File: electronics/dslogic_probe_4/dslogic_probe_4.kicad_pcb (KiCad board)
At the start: 2 copper layers, 16 parts, among them J1 Conn_02x04_Odd_Even, J2 Conn_02x04_Odd_Even

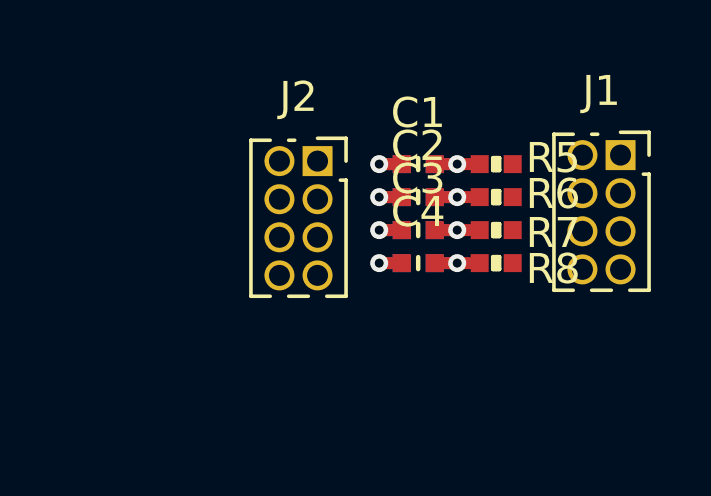
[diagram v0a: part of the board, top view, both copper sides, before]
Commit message: edge footprints for probes
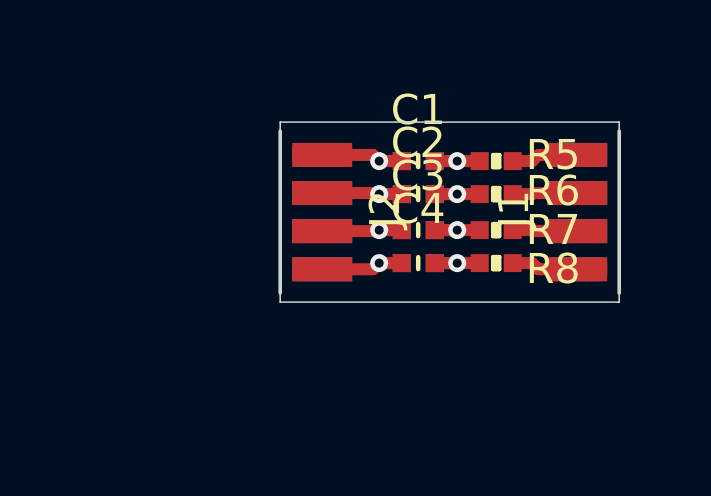
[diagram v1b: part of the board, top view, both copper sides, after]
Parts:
- J1, J2: footprint Connector_PinSocket_1.27mm:PinSocket_2x04_P1.27mm_Vertical -> SquantorConnectors:Header-0127-2X04-EDGE
- moved J1 3.18 mm to (161.6, 77.0), turned to 90 degrees
- moved J2 2.11 mm to (155.3, 77.0), turned to -90 degrees
- moved C1 0.10 mm to (157.4, 75.3)
- moved R1 0.10 mm to (157.4, 75.3)
- moved R5 0.10 mm to (160.0, 75.3)
- moved C2 0.10 mm to (157.4, 76.4)
- moved R2 0.10 mm to (157.4, 76.4)
- moved R6 0.10 mm to (160.0, 76.4)
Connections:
- C3 pad 1: Net-(C3-Pad1) -> Net-(J2-Pad6)
- J1 pad 2: Net-(R5-Pad2) -> Net-(R8-Pad2)
- J1 pad 4: Net-(R6-Pad2) -> Net-(R7-Pad2)
- J1 pad 6: Net-(R7-Pad2) -> Net-(R6-Pad2)
- J1 pad 8: Net-(R8-Pad2) -> Net-(R5-Pad2)
- J2 pad 1: Net-(C1-Pad1) -> /GND
- J2 pad 2: /GND -> Net-(C1-Pad1)
- J2 pad 3: Net-(C2-Pad1) -> /GND
- J2 pad 4: /GND -> Net-(C2-Pad1)
- J2 pad 5: Net-(C3-Pad1) -> /GND
- J2 pad 6: /GND -> Net-(J2-Pad6)
- J2 pad 7: Net-(C4-Pad1) -> /GND
- J2 pad 8: /GND -> Net-(C4-Pad1)
- R3 pad 1: Net-(C3-Pad1) -> Net-(J2-Pad6)
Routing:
- net Net-(J2-Pad6): track 0.00 -> 3.41 mm, vias 0 -> 1
- net Net-(R8-Pad2): track 0.00 -> 2.23 mm
- net Net-(R5-Pad2): track 0.00 -> 2.23 mm
- net Net-(R7-Pad2): track 0.00 -> 2.16 mm
- net Net-(R6-Pad2): track 0.00 -> 2.16 mm
- net Net-(C4-Pad1): track 1.50 -> 3.48 mm
- net Net-(C1-Pad1): track 1.50 -> 3.48 mm
- net Net-(C2-Pad1): track 1.50 -> 3.41 mm
- net Net-(C3-Pad1): track 1.50 -> 0.00 mm, vias 1 -> 0
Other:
- board outline added: 11.3 x 6 mm

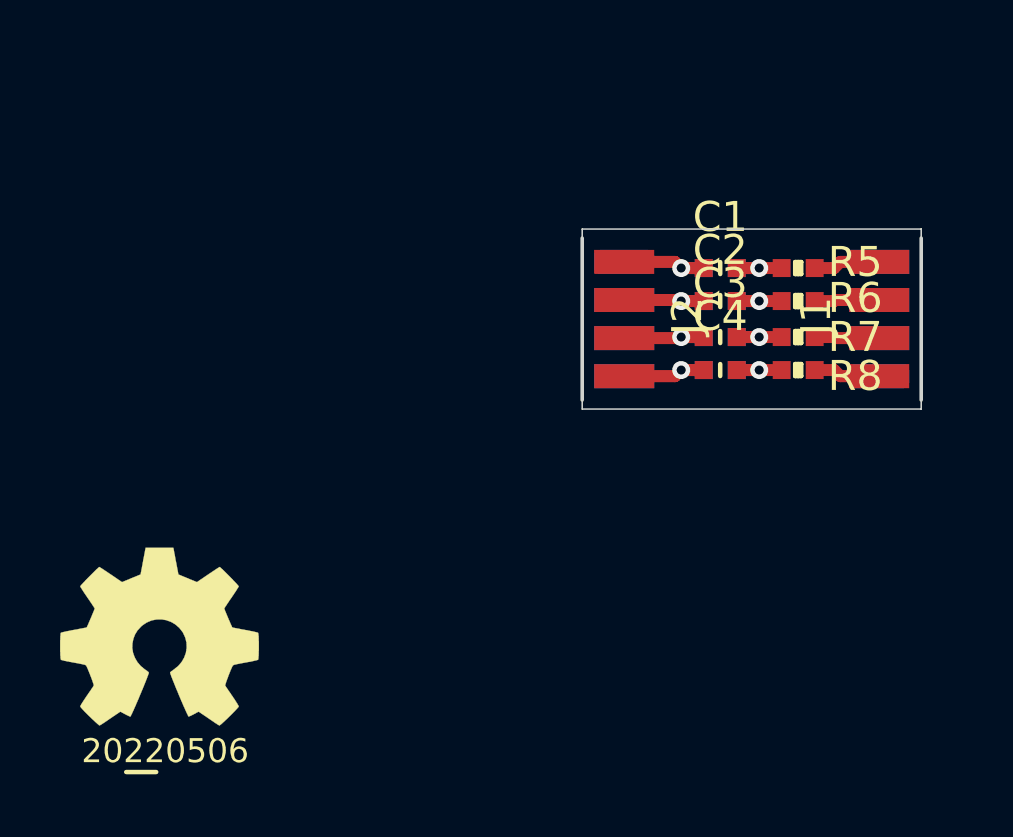
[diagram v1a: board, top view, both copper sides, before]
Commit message: added labels
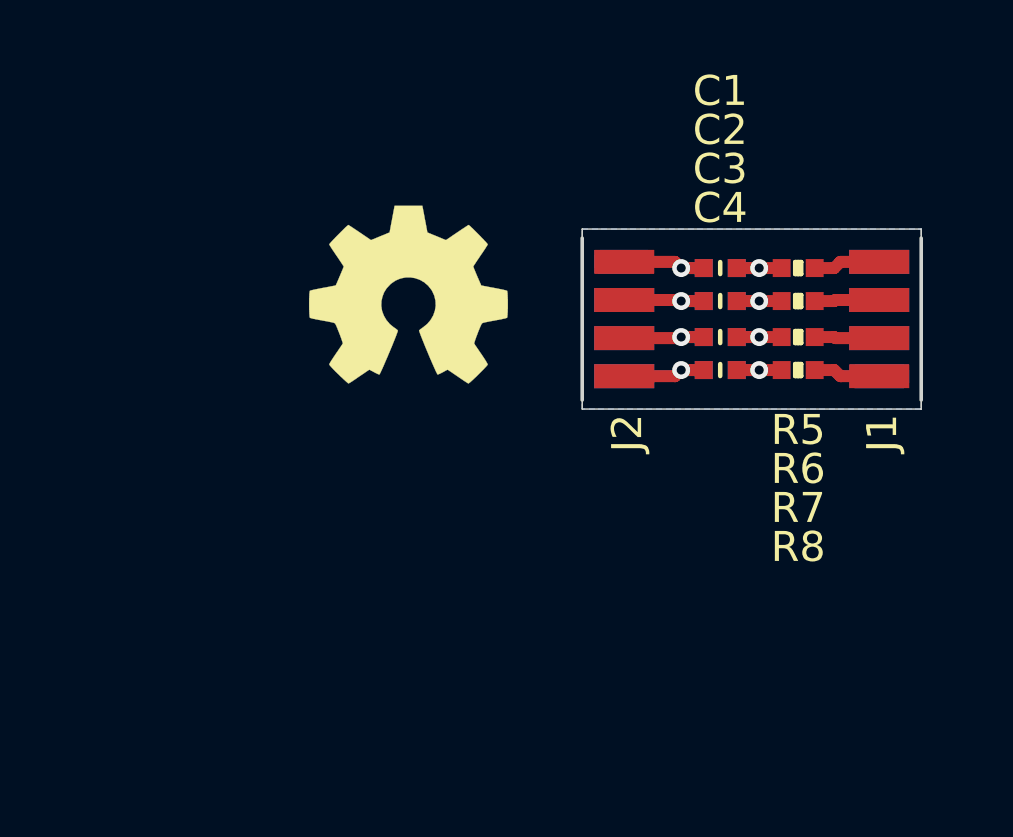
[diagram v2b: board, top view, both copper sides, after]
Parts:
- N1: moved to B.Cu
- moved N1 26.4 mm to (159.6, 76.2), turned to -90 degrees
- moved N2 14.1 mm to (147.0, 76.2)
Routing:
- added copper zone on B.Cu, net /GND
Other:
- board text added: "GND"

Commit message: made unplaceable labels invisible
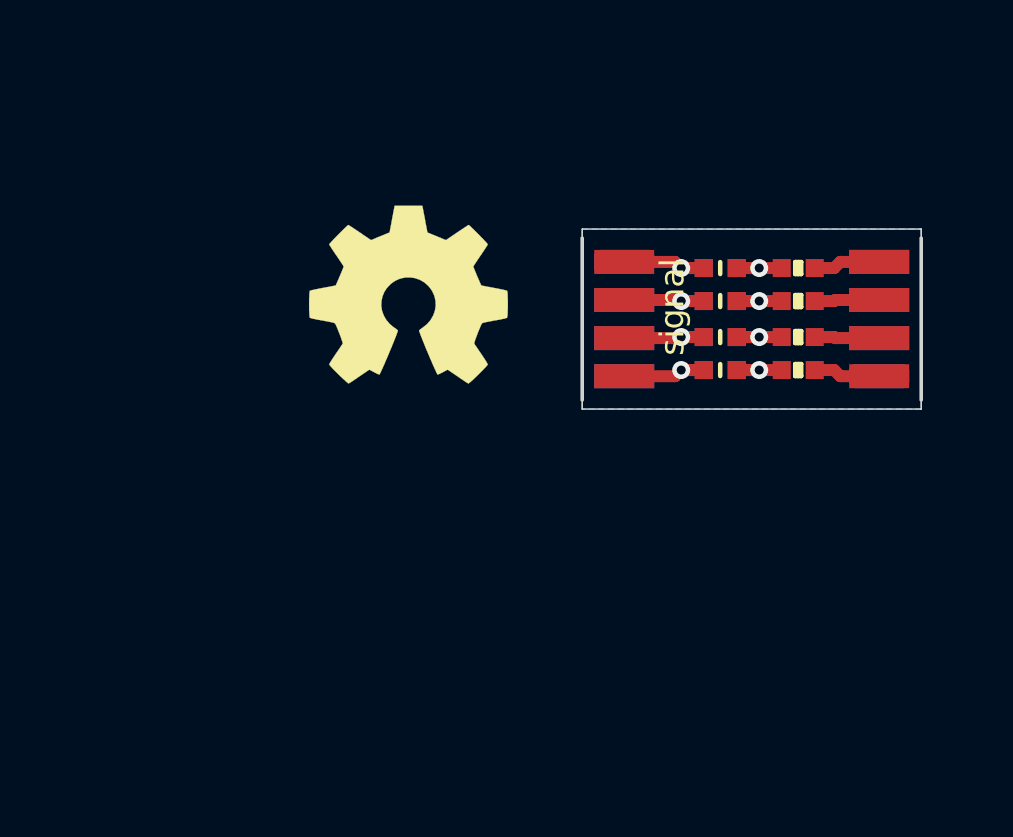
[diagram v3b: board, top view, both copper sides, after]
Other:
- board text added: "signal"
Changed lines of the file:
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@@
     (property "Sheetname" "")
     (attr smd)
-    (fp_text reference "C2" (at 0 -5.7) (layer "F.SilkS")
-      (effects (font (size 1 1) (thickness 0.15)))
-    )
-    (fp_text value "100p" (at 0 -5.7) (layer "F.Fab")
+    (fp_text reference "C2" (at 0 -5.7) (layer "F.Fab")
+      (effects (font (size 1 1) (thickness 0.15)))
+    )
+    (fp_text value "100p" (at -2.8 -5.7) (layer "F.Fab")
       (effects (font (size 1 1) (thickness 0.15)))
     )
@@
     (property "Sheetname" "")
     (attr smd)
-    (fp_text reference "J2" (at 3.8 1 90) (layer "F.SilkS")
+    (fp_text reference "J2" (at 3.8 2.3 90) (layer "F.Fab")
       (effects (font (size 1 1) (thickness 0.15)))
     )
@@
     (property "Sheetname" "")
     (attr smd)
-    (fp_text reference "J1" (at -3.8 1.2 90) (layer "F.SilkS")
+    (fp_text reference "J1" (at -3.8 2.5 90) (layer "F.Fab")
       (effects (font (size 1 1) (thickness 0.15)))
     )
@@
     (property "Sheetname" "")
     (attr smd)
-    (fp_text reference "C3" (at 0 -5.6) (layer "F.SilkS")
-      (effects (font (size 1 1) (thickness 0.15)))
-    )
-    (fp_text value "100p" (at 0 -5.6) (layer "F.Fab")
+    (fp_text reference "C3" (at 0 -5.6) (layer "F.Fab")
+      (effects (font (size 1 1) (thickness 0.15)))
+    )
+    (fp_text value "100p" (at -2.8 -5.6) (layer "F.Fab")
       (effects (font (size 1 1) (thickness 0.15)))
     )
@@
     (property "Sheetname" "")
     (attr smd)
-    (fp_text reference "R7" (at 0 5.7) (layer "F.SilkS")
+    (fp_text reference "R7" (at 2.4 5.7) (layer "F.Fab")
       (effects (font (size 1 1) (thickness 0.15)))
     )
@@
     (property "Sheetname" "")
     (attr smd)
-    (fp_text reference "C1" (at 0 -5.9) (layer "F.SilkS")
-      (effects (font (size 1 1) (thickness 0.15)))
-    )
-    (fp_text value "100p" (at 0 -5.9) (layer "F.Fab")
+    (fp_text reference "C1" (at 0 -5.9) (layer "F.Fab")
+      (effects (font (size 1 1) (thickness 0.15)))
+    )
+    (fp_text value "100p" (at -2.8 -5.9) (layer "F.Fab")
       (effects (font (size 1 1) (thickness 0.15)))
     )
@@
     (property "Sheetname" "")
     (attr smd)
-    (fp_text reference "R5" (at 0 5.4) (layer "F.SilkS")
+    (fp_text reference "R5" (at 2.4 5.4) (layer "F.Fab")
       (effects (font (size 1 1) (thickness 0.15)))
     )
@@
     (property "Sheetname" "")
     (attr smd)
-    (fp_text reference "R6" (at 0 5.6) (layer "F.SilkS")
+    (fp_text reference "R6" (at 2.4 5.6) (layer "F.Fab")
       (effects (font (size 1 1) (thickness 0.15)))
     )
@@
     (property "Sheetname" "")
     (attr smd)
-    (fp_text reference "C4" (at 0 -5.4) (layer "F.SilkS")
-      (effects (font (size 1 1) (thickness 0.15)))
-    )
-    (fp_text value "100p" (at 0 -5.4) (layer "F.Fab")
+    (fp_text reference "C4" (at 0 -5.4) (layer "F.Fab")
+      (effects (font (size 1 1) (thickness 0.15)))
+    )
+    (fp_text value "100p" (at -2.8 -5.4) (layer "F.Fab")
       (effects (font (size 1 1) (thickness 0.15)))
     )
@@
     (property "Sheetname" "")
     (attr smd)
-    (fp_text reference "R8" (at 0 5.9) (layer "F.SilkS")
+    (fp_text reference "R8" (at 2.4 5.9) (layer "F.Fab")
       (effects (font (size 1 1) (thickness 0.15)))
     )
@@
     (property "Sheetname" "")
     (attr smd)
-    (fp_text reference "R1" (at 0 5.4) (layer "B.SilkS")
+    (fp_text reference "R1" (at -2.8 5.4) (layer "B.Fab")
       (effects (font (size 1 1) (thickness 0.15)) (justify mirror))
     )
@@
     (property "Sheetname" "")
     (attr smd)
-    (fp_text reference "R3" (at 0 5.7) (layer "B.SilkS")
+    (fp_text reference "R3" (at -2.8 5.7) (layer "B.Fab")
       (effects (font (size 1 1) (thickness 0.15)) (justify mirror))
     )
@@
     (property "Sheetname" "")
     (attr smd)
-    (fp_text reference "R4" (at 0 5.9) (layer "B.SilkS")
+    (fp_text reference "R4" (at -2.8 5.9) (layer "B.Fab")
       (effects (font (size 1 1) (thickness 0.15)) (justify mirror))
     )
@@
     (property "Sheetname" "")
     (attr smd)
-    (fp_text reference "R2" (at 0 5.6) (layer "B.SilkS")
+    (fp_text reference "R2" (at -2.8 5.6) (layer "B.Fab")
       (effects (font (size 1 1) (thickness 0.15)) (justify mirror))
     )
@@
     (effects (font (size 0.8 0.8) (thickness 0.12)) (justify mirror))
   )
+  (gr_text "signal" (at 155.8 76.6 90) (layer "F.SilkS")
+    (effects (font (size 0.8 0.8) (thickness 0.12)))
+  )
   (segment (start 156.85 75.3) (end 156.1 75.3) (width 0.4) (layer "F.Cu") (net 1))

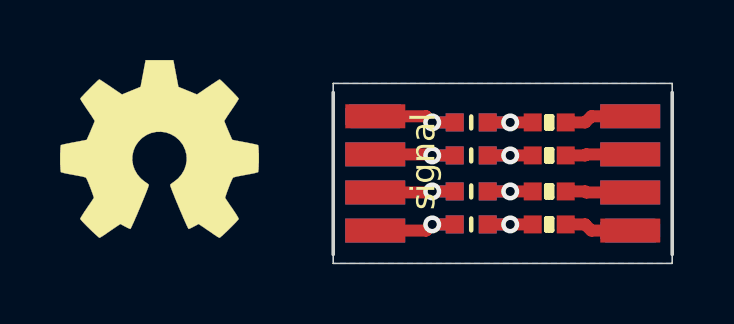
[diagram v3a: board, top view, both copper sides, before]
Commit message: updated pinout
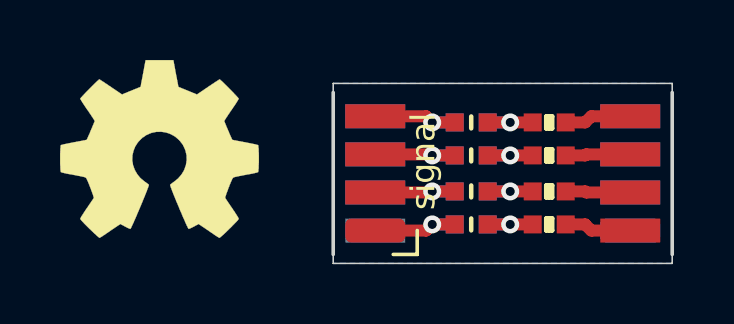
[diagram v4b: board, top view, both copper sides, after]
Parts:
- J2: moved to B.Cu
- turned J2 to 90 degrees
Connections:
- C3 pad 1: Net-(J2-Pad6) -> Net-(J2-Pad3)
- C4 pad 1: Net-(C4-Pad1) -> Net-(J2-Pad1)
- J2 pad 1: /GND -> Net-(J2-Pad1)
- J2 pad 2: Net-(C1-Pad1) -> /GND
- J2 pad 3: /GND -> Net-(J2-Pad3)
- J2 pad 4: Net-(C2-Pad1) -> /GND
- J2 pad 5: /GND -> Net-(C2-Pad1)
- J2 pad 6: Net-(J2-Pad6) -> /GND
- J2 pad 7: /GND -> Net-(C1-Pad1)
- J2 pad 8: Net-(C4-Pad1) -> /GND
- R3 pad 1: Net-(J2-Pad6) -> Net-(J2-Pad3)
- R4 pad 1: Net-(C4-Pad1) -> Net-(J2-Pad1)
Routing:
- net Net-(J2-Pad1): track 0.00 -> 3.48 mm, vias 0 -> 1
- net Net-(C4-Pad1): track 3.48 -> 0.00 mm, vias 1 -> 0
- net Net-(J2-Pad6): track 3.41 -> 0.00 mm, vias 1 -> 0
- net Net-(J2-Pad3): track 0.00 -> 3.41 mm, vias 0 -> 1
